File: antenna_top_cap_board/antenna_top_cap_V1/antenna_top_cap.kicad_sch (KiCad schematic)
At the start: 29 parts, among them IC1 PCT2075DP,118, J1 Battery Charge Bypass, J2 Battery Charge Bypass, J3 Burn_Wire, J6 Conn_Coaxial, J7 Breakout, Q1 BSS138, U1 VL6180XV0NR/1, U2 LP5907-2.8V, U3 0433BM15A0001

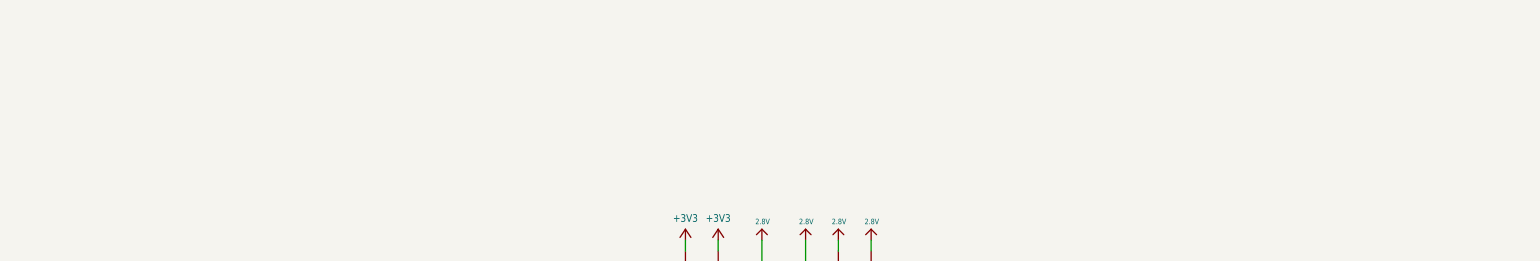
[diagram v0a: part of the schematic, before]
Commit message: Antenna Top Cap for Development Board
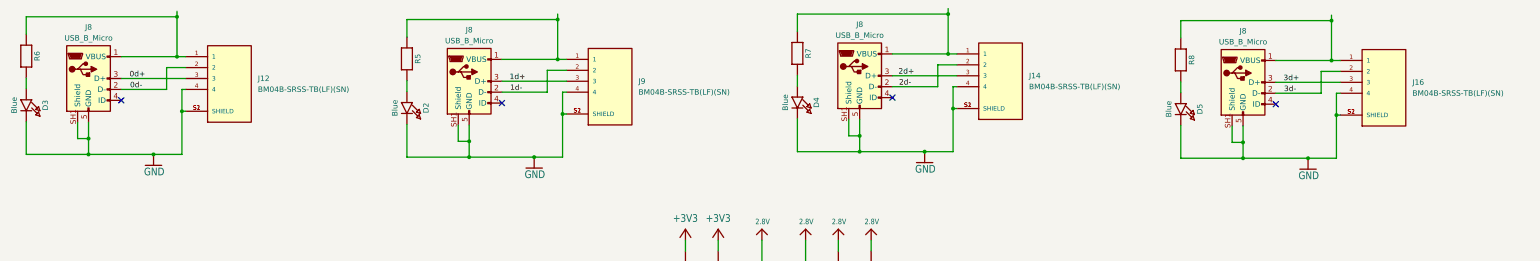
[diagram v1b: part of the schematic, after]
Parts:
- added D2, D3, D4, D5: Blue, LED_SMD:LED_0603_1608Metric, symbol Adafruit ItsyBitsy RP2040-eagle-import:LED0603_NOOUTLINE
- added J12, J14, J16, J9: BM04B-SRSS-TB(LF)(SN), Antenna_board:JST_BM04B-SRSS-TB(LF)(SN), symbol BM04B-SRSS-TB_LF__SN_:BM04B-SRSS-TB(LF)(SN)
- added J8 (x4): USB_B_Micro, Antenna_board:MOLEX_105164-0001, symbol Connector:USB_B_Micro
- added R5, R6, R7, R8: 1K, Resistor_SMD:R_0402_1005Metric, symbol Adafruit ItsyBitsy RP2040-eagle-import:RESISTOR_0402NO
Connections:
- net GND: now also D2.2 (C), D3.2 (C), D4.2 (C), D5.2 (C), J12.4, J12.S1 (SHIELD), J12.S2 (SHIELD), J14.4, J14.S1 (SHIELD), J14.S2 (SHIELD), J16.4, J16.S1 (SHIELD), J16.S2 (SHIELD), J8.5 (GND), J8.5 (GND), J8.5 (GND), J8.5 (GND), J8.SH1 (Shield), J8.SH1 (Shield), J8.SH1 (Shield), J8.SH1 (Shield), J9.4, J9.S1 (SHIELD), J9.S2 (SHIELD)
- new net: J12.1, J8.1 (VBUS), R6.1
- new net: J16.1, J8.1 (VBUS), R8.1
- new net: D5.1 (A), R8.2
- new net: D3.1 (A), R6.2
- new net: J14.1, J8.1 (VBUS), R7.1
- new net: J8.1 (VBUS), J9.1, R5.1
- new net: D2.1 (A), R5.2
- new net: D4.1 (A), R7.2
- new net 0d+: J12.3, J8.3 (D+)
- new net 0d-: J12.2, J8.2 (D-)
- new net 1d+: J8.3 (D+), J9.3
- new net 1d-: J8.2 (D-), J9.2
- new net 2d+: J14.3, J8.3 (D+)
- new net 2d-: J14.2, J8.2 (D-)
- new net 3d+: J16.3, J8.3 (D+)
- new net 3d-: J16.2, J8.2 (D-)
- no-connect marks 1 -> 5
